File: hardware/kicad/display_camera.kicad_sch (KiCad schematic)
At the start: 8 parts, among them J3 DSI1 22p 0.5mm (Waveshare 4.3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, J4 CSI0 22p 0.5mm (Camera Module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

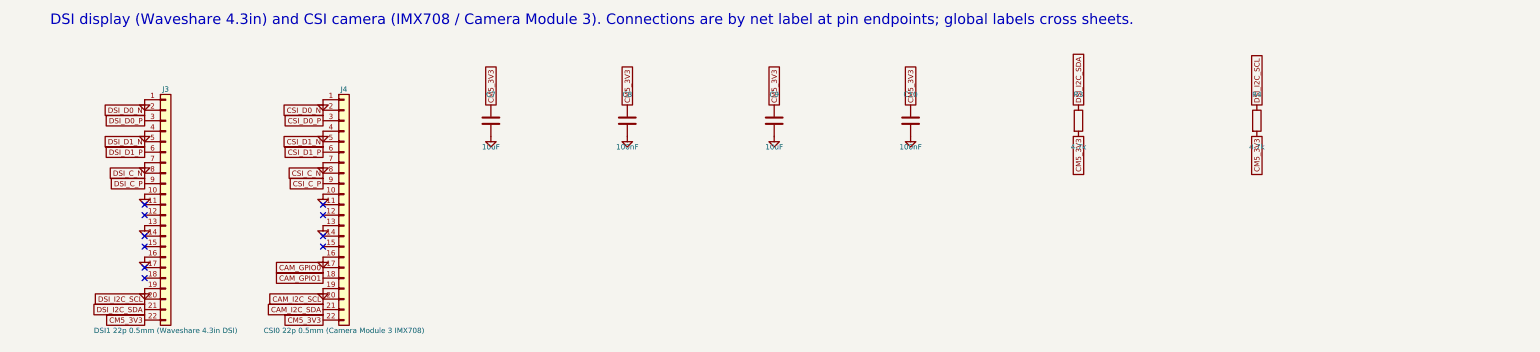
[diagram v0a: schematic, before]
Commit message: Sync KiCad schematic to netlist v3.2; add side_flex sheet
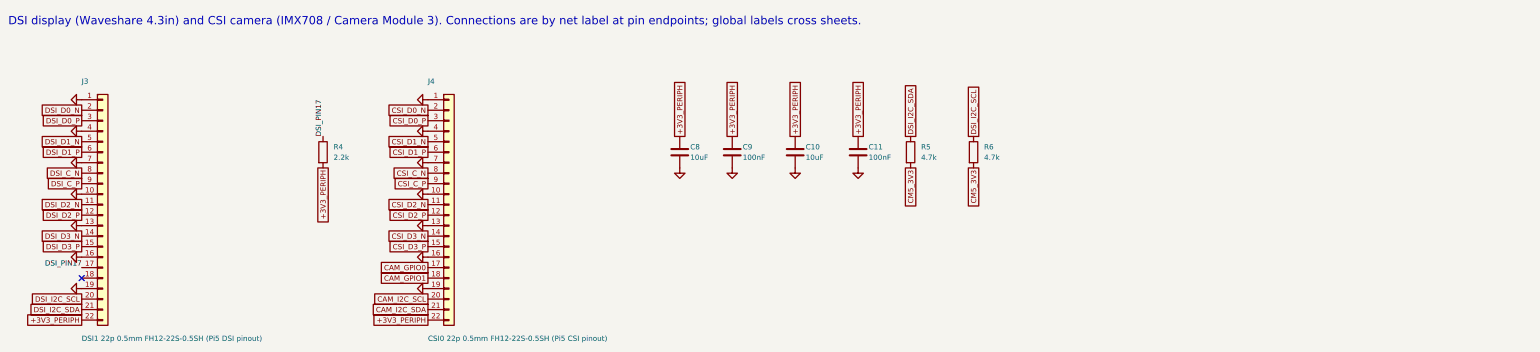
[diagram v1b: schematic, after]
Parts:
- removed C7: 10uF, Capacitor_SMD:C_0603_1608Metric, symbol Device:C
- removed R3: 4.7k, Resistor_SMD:R_0402_1005Metric, symbol Device:R
- added C11: 100nF, Capacitor_SMD:C_0402_1005Metric, symbol Device:C
- added R5, R6: 4.7k, Resistor_SMD:R_0402_1005Metric, symbol Device:R
- C10, C8: value 100nF -> 10uF; footprint Capacitor_SMD:C_0402_1005Metric -> Capacitor_SMD:C_0603_1608Metric
- C9: value 10uF -> 100nF; footprint Capacitor_SMD:C_0603_1608Metric -> Capacitor_SMD:C_0402_1005Metric
- J3: value DSI1 22p 0.5mm (Waveshare 4.3in DSI) -> DSI1 22p 0.5mm FH12-22S-0.5SH (Pi5 DSI pinout)
- J4: value CSI0 22p 0.5mm (Camera Module 3 IMX708) -> CSI0 22p 0.5mm FH12-22S-0.5SH (Pi5 CSI pinout)
- R4: value 4.7k -> 2.2k
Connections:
- net CM5_3V3: now also R5.2, R6.2; no longer C10.1, C8.1, C9.1, J3.22 (Pin_22), J4.22 (Pin_22), R4.2
- net DSI_I2C_SCL: now also R6.1; no longer R4.1
- net DSI_I2C_SDA: now also R5.1
- net GND: now also C11.2
- net DSI_D2_N: now reaches J3.11 (Pin_11)
- net DSI_D2_P: now reaches J3.12 (Pin_12)
- net DSI_D3_N: now reaches J3.14 (Pin_14)
- net DSI_D3_P: now reaches J3.15 (Pin_15)
- net DSI_PIN17: now reaches J3.17 (Pin_17)
- net DSI_PIN17: now also R4.1
- net CSI_D2_N: now reaches J4.11 (Pin_11)
- net CSI_D2_P: now reaches J4.12 (Pin_12)
- net CSI_D3_N: now reaches J4.14 (Pin_14)
- net CSI_D3_P: now reaches J4.15 (Pin_15)
- new net +3V3_PERIPH: C10.1, C11.1, C8.1, C9.1, J3.22 (Pin_22), J4.22 (Pin_22), R4.2
- no-connect marks 10 -> 1
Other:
- title: PocketMate - DSI display (Waveshare 4.3in) and CSI camera (IMX708 / Camera Module 3) -> PocketMate - DisplayCamera
